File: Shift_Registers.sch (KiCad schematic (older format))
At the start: 4 parts, among them U14 74HC595, U15 74HC595, U16 74HC595, U17 74HC595

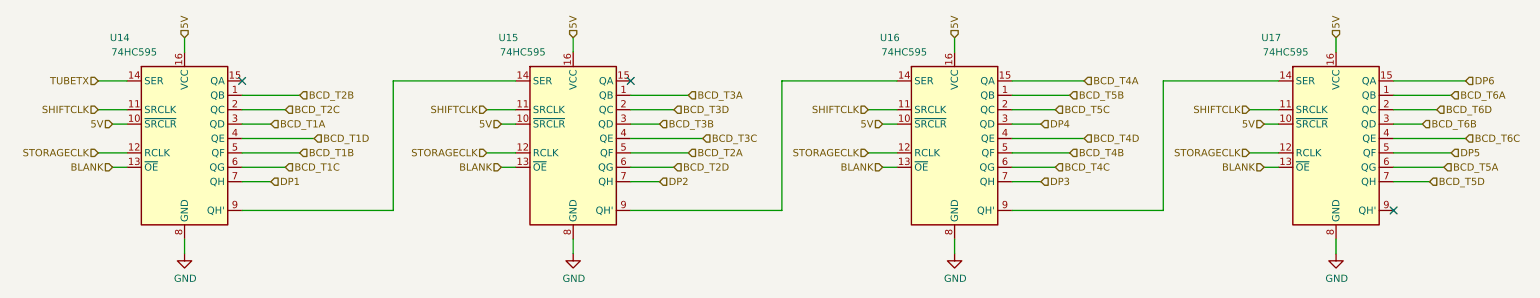
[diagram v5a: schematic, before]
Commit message: Fixed tube footprints and rerouted
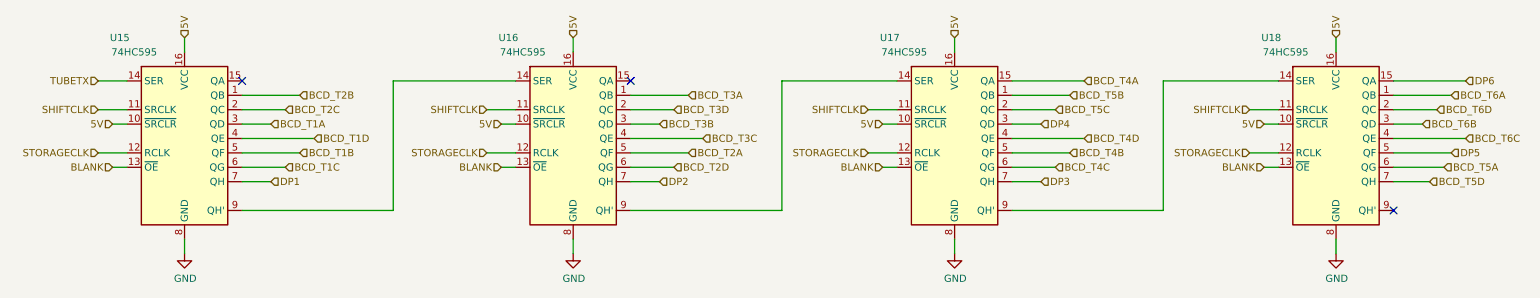
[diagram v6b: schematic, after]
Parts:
- renumbered U14 to U15, U15 to U16, U16 to U17, U17 to U18
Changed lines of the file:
@@
 EESchema Schematic File Version 4
-LIBS:nixieClock_ZM1000-cache
 EELAYER 30 0
 EELAYER END
@@
 BCD_T3D
 $Comp
-L 74xx:74HC595 U14
+L 74xx:74HC595 U15
 U 1 1 5DB9947F
 P 1800 3600
-F 0 "U14" H 1350 4300 50  0000 C CNN
+F 0 "U15" H 1350 4300 50  0000 C CNN
 F 1 "74HC595" H 1450 4200 50  0000 C CNN
 F 2 "Package_DIP:DIP-16_W7.62mm" H 1800 3600 50  0001 C CNN
@@
 BCD_T1A
 $Comp
-L power:GND #PWR021
+L power:GND #PWR025
 U 1 1 5DB9F4DB
 P 1800 4400
-F 0 "#PWR021" H 1800 4150 50  0001 C CNN
+F 0 "#PWR025" H 1800 4150 50  0001 C CNN
 F 1 "GND" H 1805 4227 50  0000 C CNN
 F 2 "" H 1800 4400 50  0001 C CNN
@@
 	2200 3300 2600 3300
 $Comp
-L 74xx:74HC595 U15
+L 74xx:74HC595 U16
 U 1 1 5DBA8ADB
 P 4500 3600
-F 0 "U15" H 4050 4300 50  0000 C CNN
+F 0 "U16" H 4050 4300 50  0000 C CNN
 F 1 "74HC595" H 4150 4200 50  0000 C CNN
 F 2 "Package_DIP:DIP-16_W7.62mm" H 4500 3600 50  0001 C CNN
@@
 $EndComp
 $Comp
-L power:GND #PWR022
+L power:GND #PWR026
 U 1 1 5DBA8AE1
 P 4500 4400
-F 0 "#PWR022" H 4500 4150 50  0001 C CNN
+F 0 "#PWR026" H 4500 4150 50  0001 C CNN
 F 1 "GND" H 4505 4227 50  0000 C CNN
 F 2 "" H 4500 4400 50  0001 C CNN
@@
 	4900 3300 5300 3300
 $Comp
-L 74xx:74HC595 U16
+L 74xx:74HC595 U17
 U 1 1 5DBAB05B
 P 7150 3600
-F 0 "U16" H 6700 4300 50  0000 C CNN
+F 0 "U17" H 6700 4300 50  0000 C CNN
 F 1 "74HC595" H 6800 4200 50  0000 C CNN
 F 2 "Package_DIP:DIP-16_W7.62mm" H 7150 3600 50  0001 C CNN
@@
 $EndComp
 $Comp
-L power:GND #PWR023
+L power:GND #PWR027
 U 1 1 5DBAB061
 P 7150 4400
-F 0 "#PWR023" H 7150 4150 50  0001 C CNN
+F 0 "#PWR027" H 7150 4150 50  0001 C CNN
 F 1 "GND" H 7155 4227 50  0000 C CNN
 F 2 "" H 7150 4400 50  0001 C CNN
@@
 	7550 3300 7950 3300
 $Comp
-L 74xx:74HC595 U17
+L 74xx:74HC595 U18
 U 1 1 5D93C146
 P 9800 3600
-F 0 "U17" H 9350 4300 50  0000 C CNN
+F 0 "U18" H 9350 4300 50  0000 C CNN
 F 1 "74HC595" H 9450 4200 50  0000 C CNN
 F 2 "Package_DIP:DIP-16_W7.62mm" H 9800 3600 50  0001 C CNN
@@
 $EndComp
 $Comp
-L power:GND #PWR024
+L power:GND #PWR028
 U 1 1 5D93C14C
 P 9800 4400
-F 0 "#PWR024" H 9800 4150 50  0001 C CNN
+F 0 "#PWR028" H 9800 4150 50  0001 C CNN
 F 1 "GND" H 9805 4227 50  0000 C CNN
 F 2 "" H 9800 4400 50  0001 C CNN
